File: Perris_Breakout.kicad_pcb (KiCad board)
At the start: 2 copper layers, 17 parts, among them J1 PERRI_1, J10 SCL_Microcontroller, J11 Conn_01x01_Male, J12 SCL_Microcontroller, J13 Conn_01x01_Male, J14 SCL_Microcontroller, J2 PERRI_2, J3 PERRI_3, J4 PERRI_4, J5 PERRI_5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

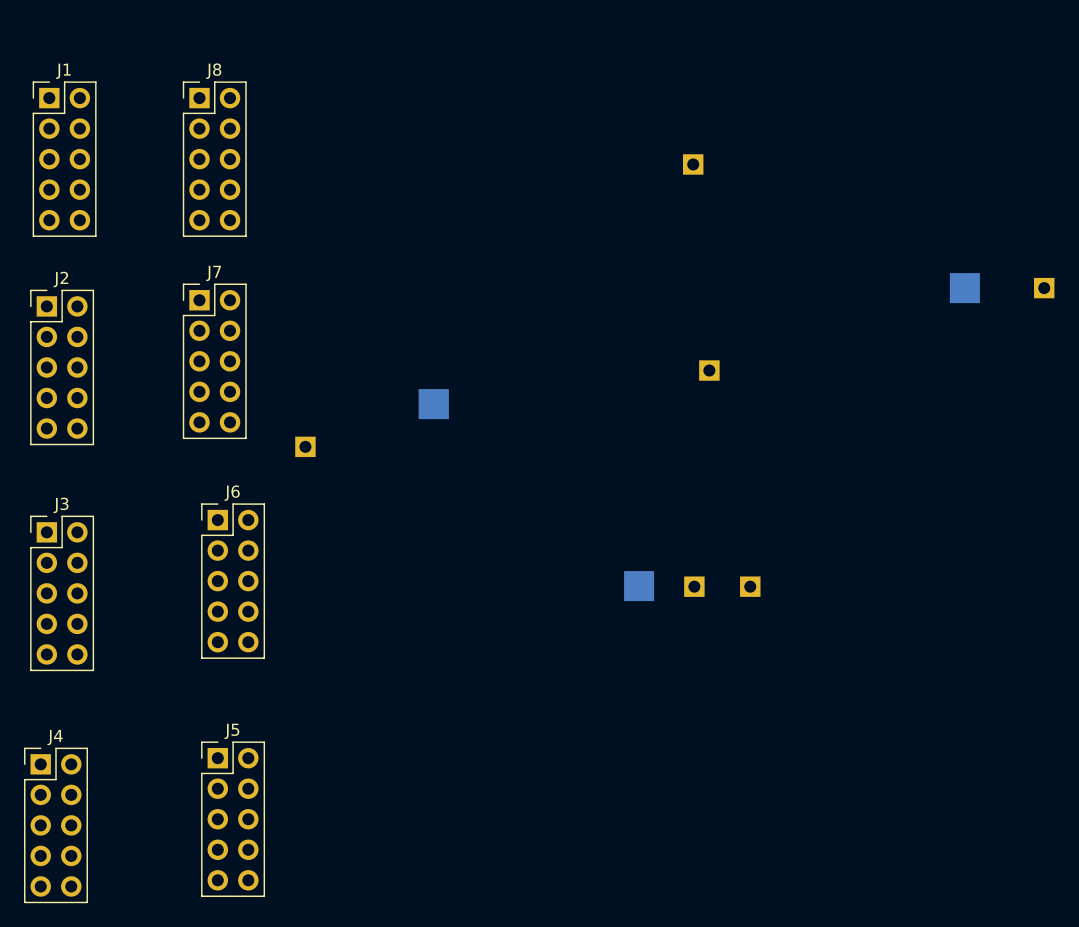
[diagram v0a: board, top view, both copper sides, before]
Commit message: Finished Perri I2C Breakout Board
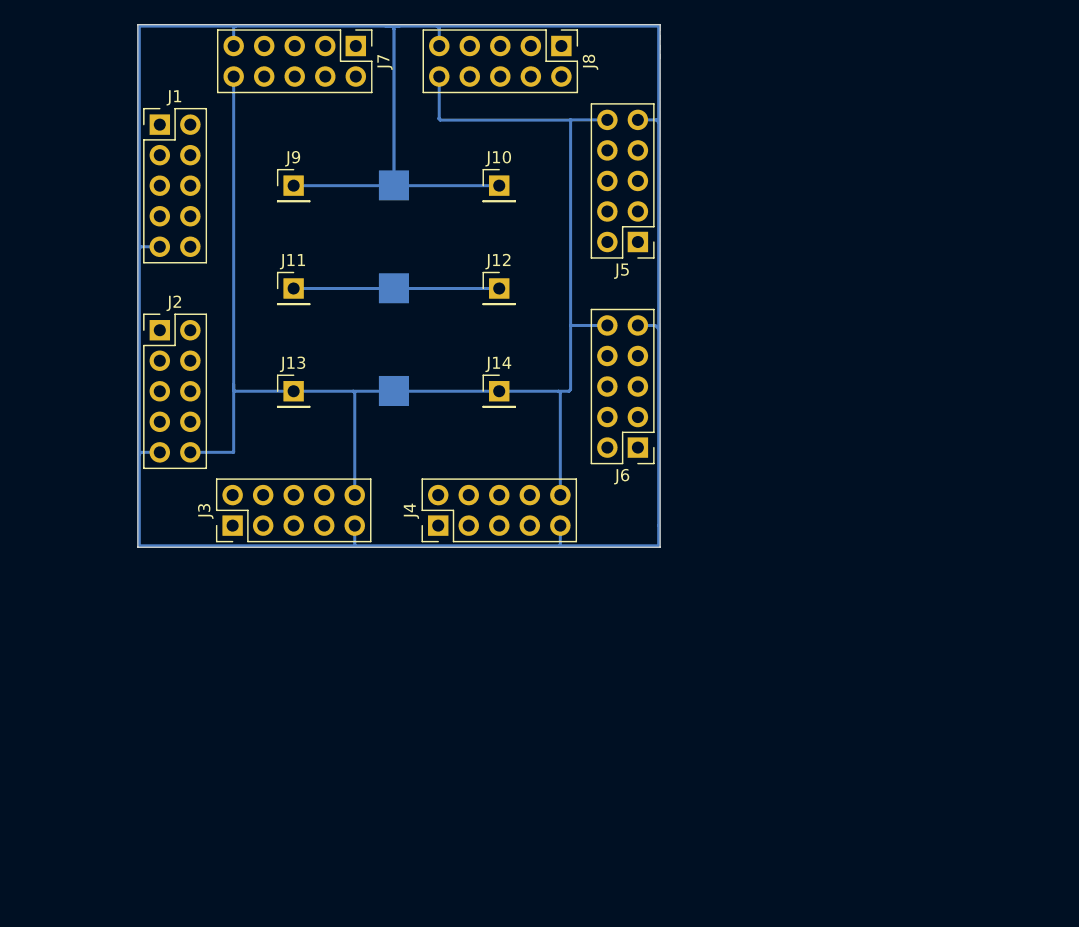
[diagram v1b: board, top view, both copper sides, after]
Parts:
- J10, J11, J12, J13, J14, J9: moved to F.Cu
- moved J9 63.0 mm to (111.5, 63.1), turned to 0 degrees
- moved J5 55.4 mm to (140.1, 67.8), turned to 180 degrees
- moved TP1 48.3 mm to (119.8, 63.1)
- moved J11 41.6 mm to (111.5, 71.7), turned to 0 degrees
- moved J4 38.6 mm to (123.5, 91.4), turned to 90 degrees
- moved J13 38.2 mm to (111.5, 80.2), turned to 0 degrees
- moved J6 35.5 mm to (140.1, 84.9), turned to 180 degrees
- moved J8 30.4 mm to (133.7, 51.5), turned to -90 degrees
- moved J10 27.1 mm to (128.6, 63.1), turned to 0 degrees
- moved J14 26.5 mm to (128.6, 80.2), turned to 0 degrees
- moved TP3 26.1 mm to (119.8, 80.2)
- moved J7 24.8 mm to (116.6, 51.5), turned to -90 degrees
- moved J12 18.8 mm to (128.6, 71.7), turned to 0 degrees
- moved J3 15.5 mm to (106.4, 91.4), turned to 90 degrees
- moved TP2 10.2 mm to (119.8, 71.6)
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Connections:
- J11 pad 1: /SDA -> /GND
- J12 pad 1: /SDA -> /GND
- J13 pad 1: /GND -> /SDA
- J14 pad 1: /GND -> /SDA
- TP2 pad 1: /SDA -> /GND
- TP3 pad 1: /GND -> /SDA
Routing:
- net /SCL: track 0.00 -> 218.6 mm
- net /SDA: track 0.00 -> 124.0 mm
- net /GND: track 0.00 -> 17.1 mm
- added copper zone on B.Cu, net /GND
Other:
- board outline added: 43.5 x 43.5 mm

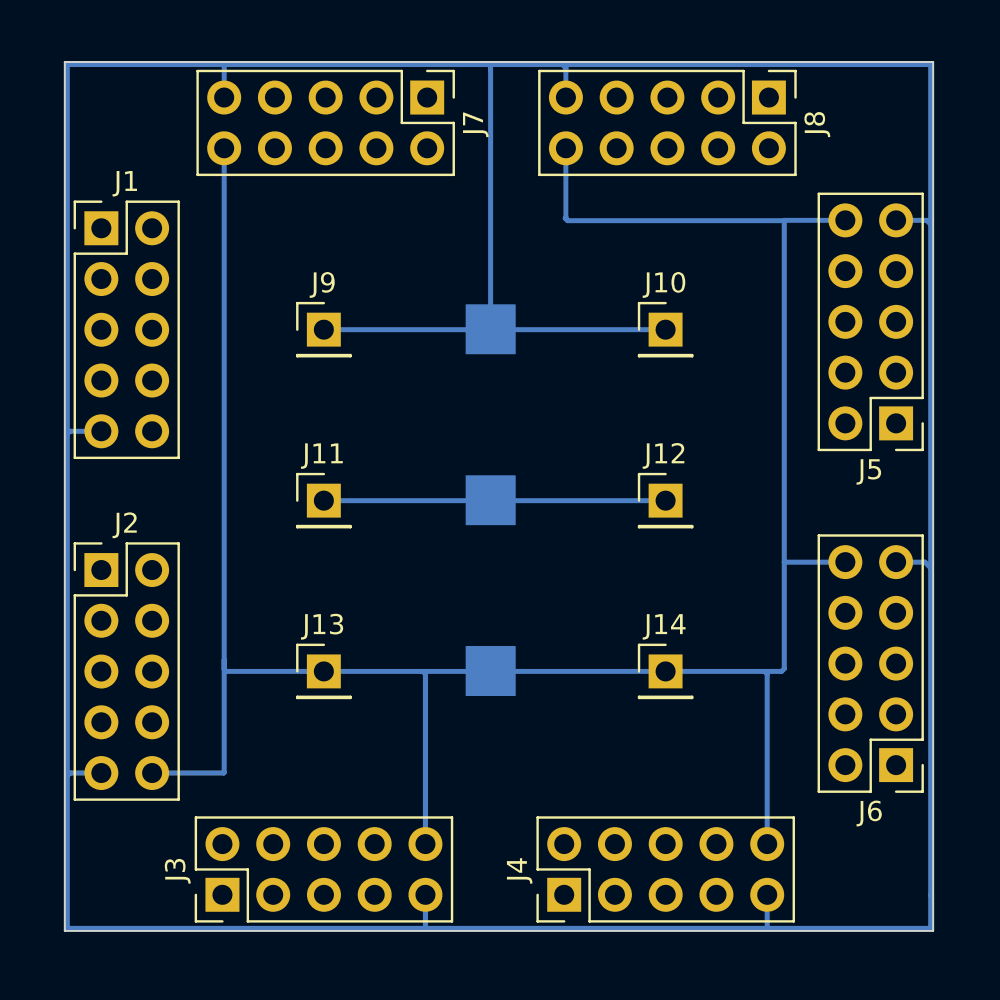
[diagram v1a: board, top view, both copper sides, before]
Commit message: Incresed track width to 50mils. Added vias to connect ground planes.
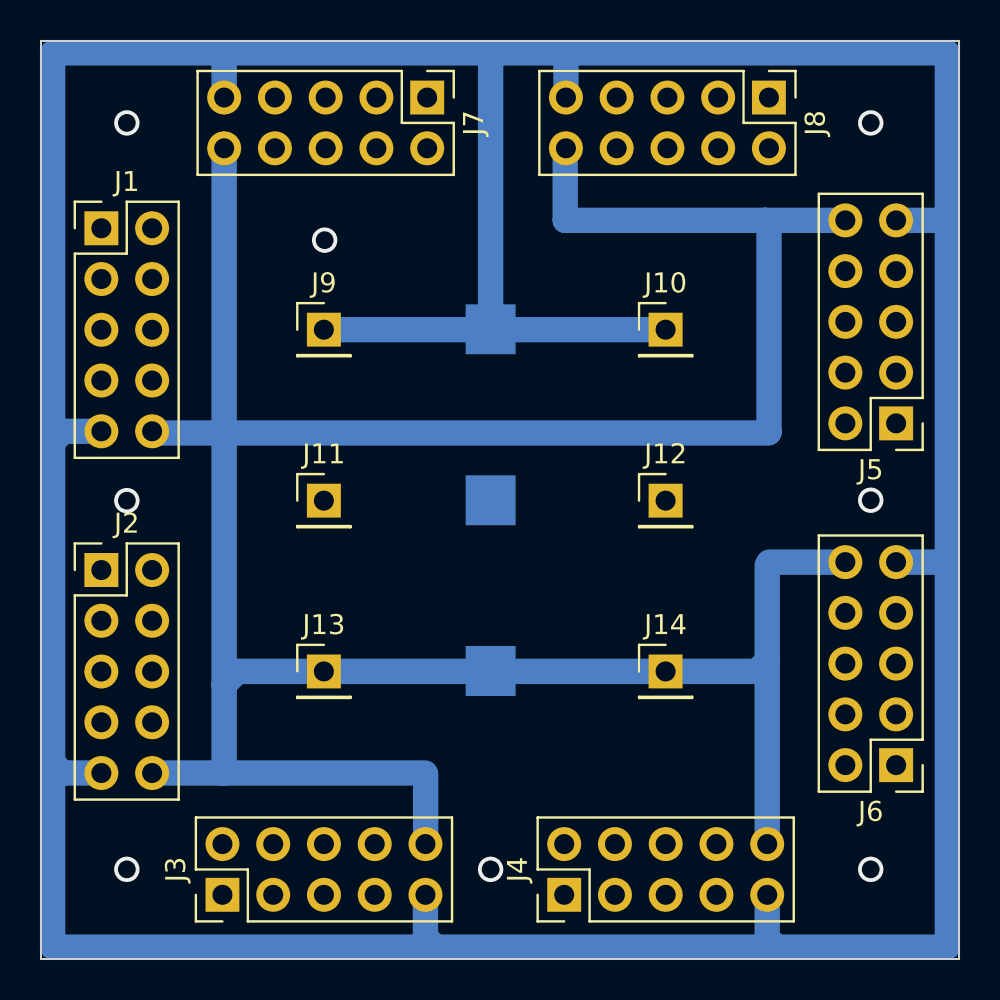
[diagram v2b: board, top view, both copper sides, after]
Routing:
- net /SDA: track 124.0 -> 153.1 mm
- net /GND: track 17.1 -> 0.00 mm, vias 0 -> 8
- net /SCL: track 218.6 -> 231.0 mm
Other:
- board size 43.5 x 43.5 mm -> 45.9 x 45.9 mm

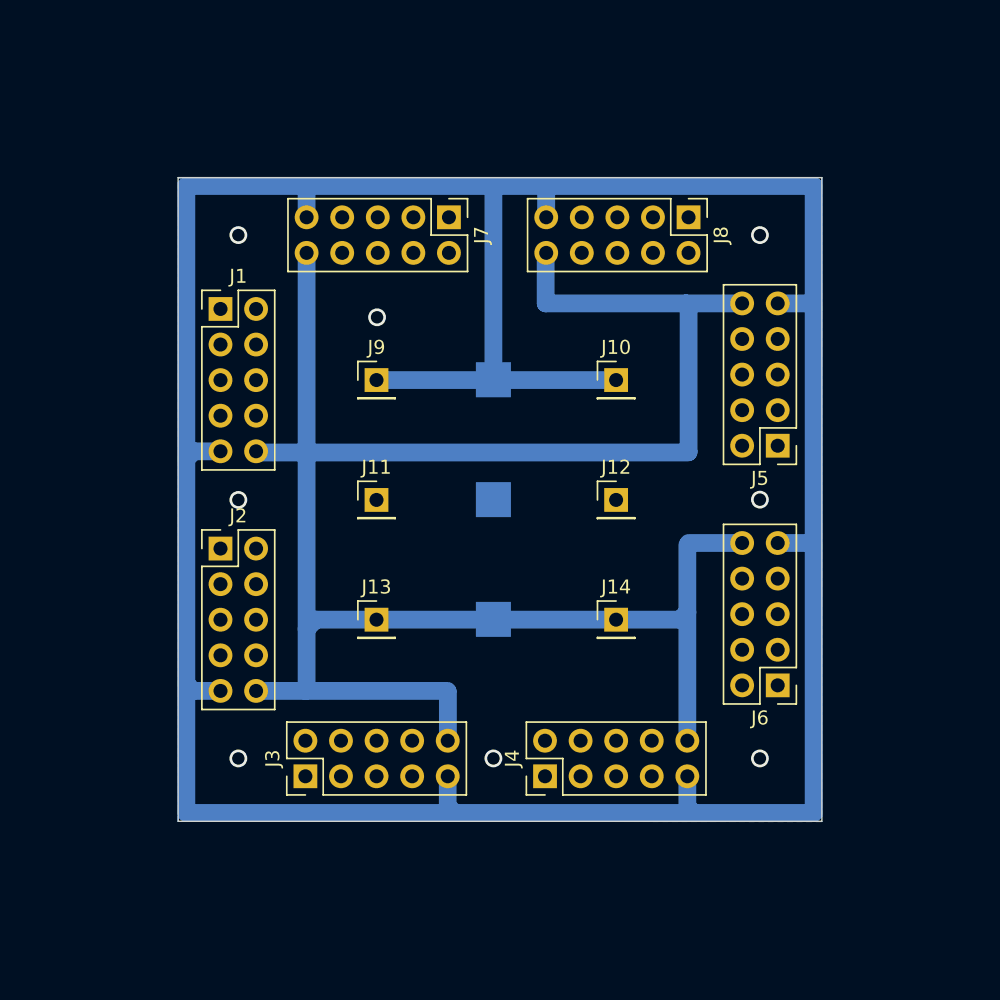
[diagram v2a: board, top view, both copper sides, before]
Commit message: Updated PCB with ground plane surroudning connectors.
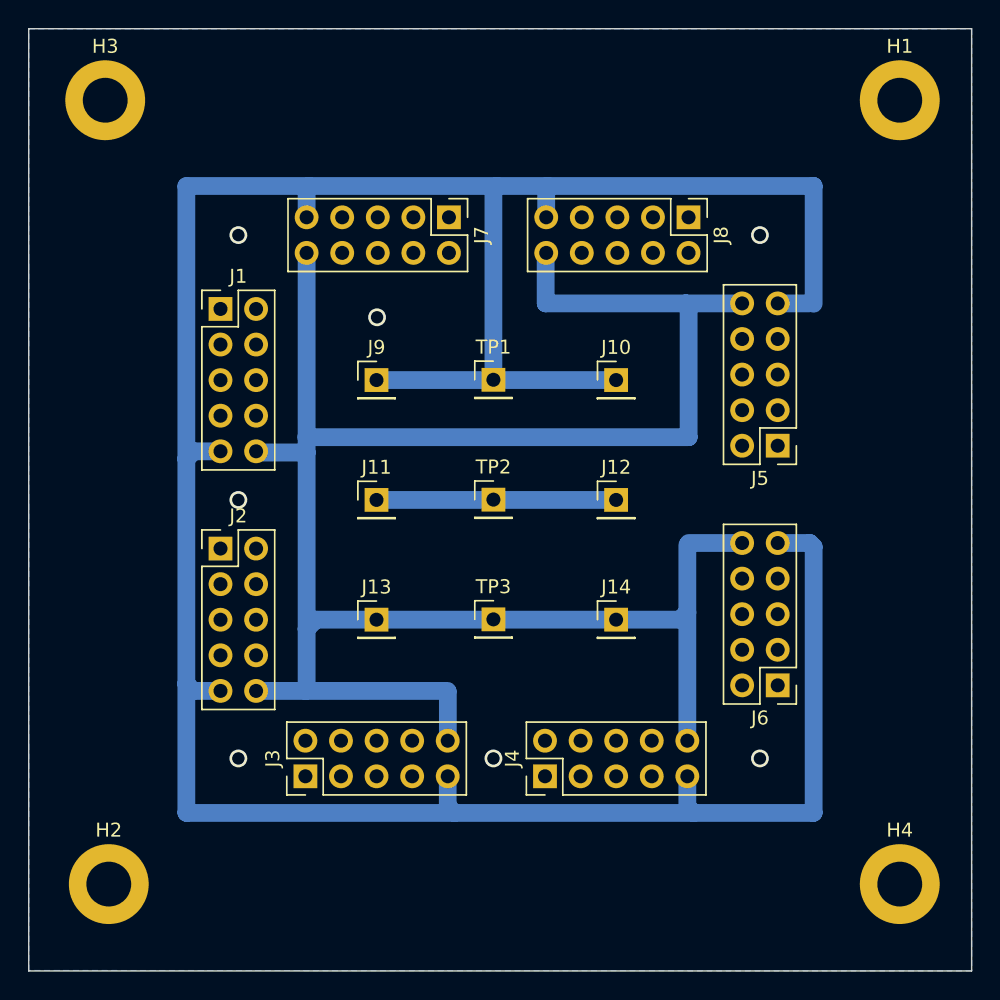
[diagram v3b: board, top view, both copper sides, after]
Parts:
- added H1: MountingHole_Pad, MountingHole:MountingHole_3.2mm_M3_ISO7380_Pad, F.Cu at (148.8, 43.1)
- added H2: MountingHole_Pad, MountingHole:MountingHole_3.2mm_M3_ISO7380_Pad, F.Cu at (92.4, 99.1)
- added H3: MountingHole_Pad, MountingHole:MountingHole_3.2mm_M3_ISO7380_Pad, F.Cu at (92.1, 43.1)
- added H4: MountingHole_Pad, MountingHole:MountingHole_3.2mm_M3_ISO7380_Pad, F.Cu at (148.8, 99.1)
- J10: value SCL_Microcontroller -> SCL
- J11: value Conn_01x01_Male -> GND
- J12: value SCL_Microcontroller -> GND
- J13: value Conn_01x01_Male -> SDA
- J14: value SCL_Microcontroller -> SDA
- J9: value Conn_01x01_Male -> SCL
- TP1: value SCL_Test -> SCL; footprint TestPoint:TestPoint_Pad_2.5x2.5mm -> Connector_PinHeader_2.54mm:PinHeader_1x01_P2.54mm_Vertical; moved to F.Cu
- TP2: value SCL_Test -> GND; footprint TestPoint:TestPoint_Pad_2.5x2.5mm -> Connector_PinHeader_2.54mm:PinHeader_1x01_P2.54mm_Vertical; moved to F.Cu
- TP3: value SCL_Test -> SDA; footprint TestPoint:TestPoint_Pad_2.5x2.5mm -> Connector_PinHeader_2.54mm:PinHeader_1x01_P2.54mm_Vertical; moved to F.Cu
- turned TP1 to 0 degrees
- turned TP2 to 0 degrees
- turned TP3 to 0 degrees
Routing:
- net /SCL: track 231.0 -> 213.1 mm
- net /GND: track 0.00 -> 17.1 mm, vias 8 -> 7
- net /SDA: track 153.1 -> 152.0 mm
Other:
- board size 45.9 x 45.9 mm -> 67.3 x 67.3 mm

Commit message: Changed copper zone properties
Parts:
- J1, J2, J3, J4, J5, J6, J7, J8: footprint HELIX:Perri_conn_2x5 -> HELIX:Perri_conn_2x5_Reverse
- J10, J9, TP1: value SCL -> SDA
- J13, J14, TP3: value SDA -> SCL
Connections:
- J10 pad 1: /SCL -> /SDA
- J13 pad 1: /SDA -> /SCL
- J14 pad 1: /SDA -> /SCL
- J9 pad 1: /SCL -> /SDA
- TP1 pad 1: /SCL -> /SDA
- TP3 pad 1: /SDA -> /SCL
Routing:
- net /SDA: track 152.0 -> 213.1 mm
- net /SCL: track 213.1 -> 152.0 mm

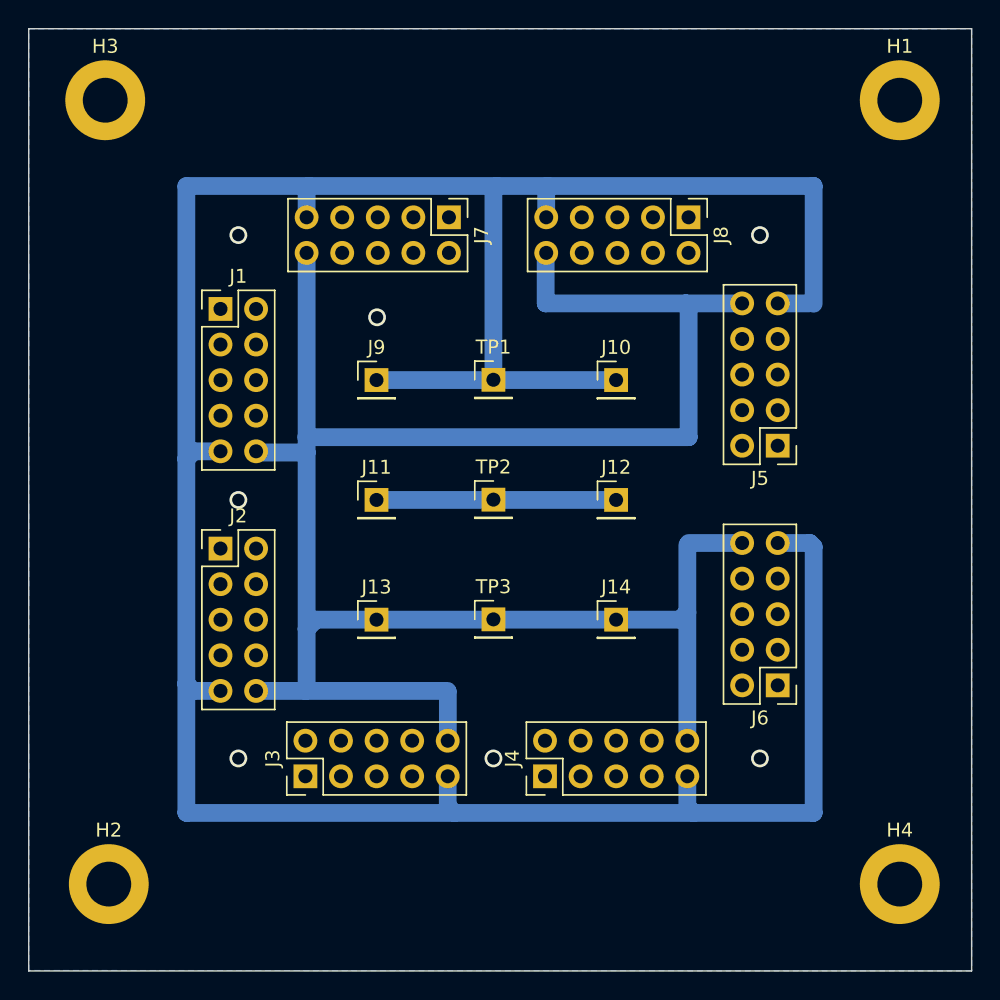
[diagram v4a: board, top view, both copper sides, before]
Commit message: Added second copper layer for ground
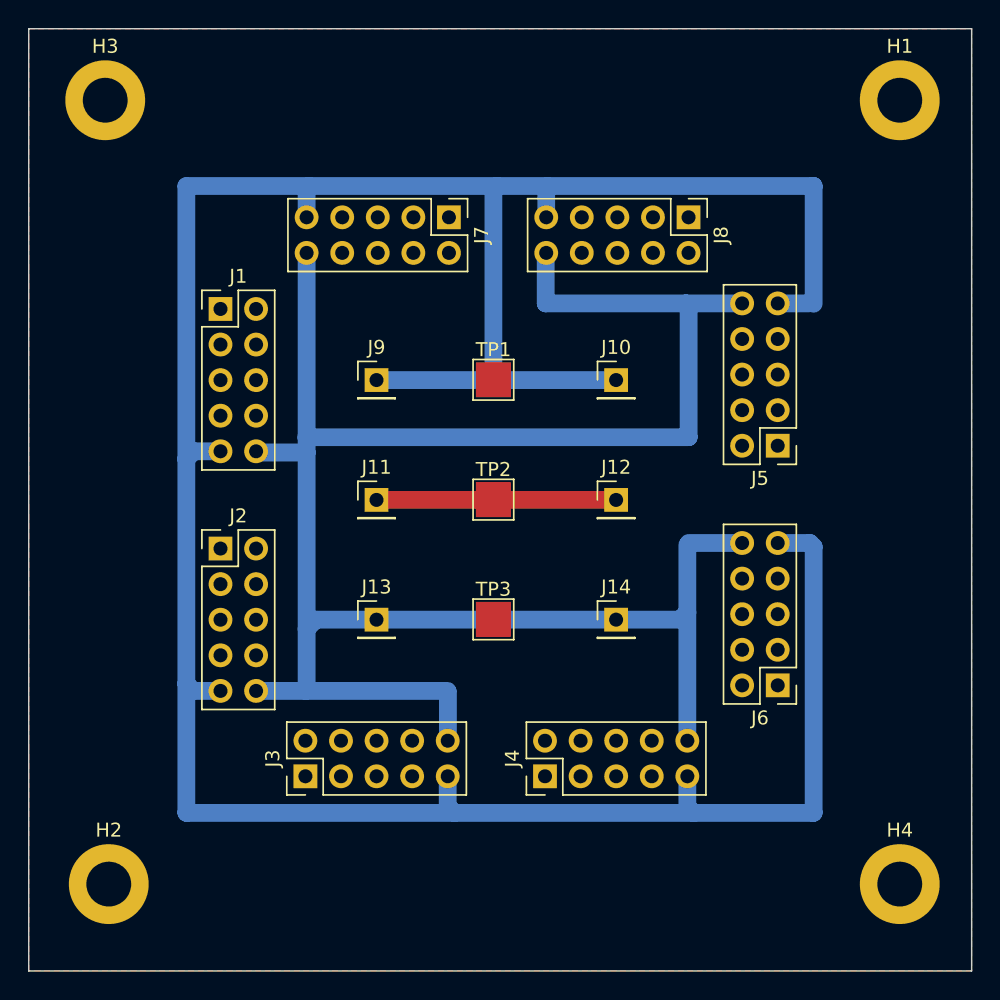
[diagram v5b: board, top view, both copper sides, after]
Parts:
- TP1, TP2, TP3: footprint Connector_PinHeader_2.54mm:PinHeader_1x01_P2.54mm_Vertical -> TestPoint:TestPoint_Pad_2.5x2.5mm
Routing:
- net /GND: vias 7 -> 0
- added copper zone on F.Cu, net /GND
- removed copper zone on B.Cu, net /GND
